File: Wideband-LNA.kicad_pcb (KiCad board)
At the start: 4 copper layers, 23.9 x 22.5 mm, 23 parts, among them J1 Conn_Coaxial, J2 Conn_Coaxial, J3 USB_C_Receptacle_USB2.0_16P, U1 TQP3M9037, U2 AP2127K-ADJ

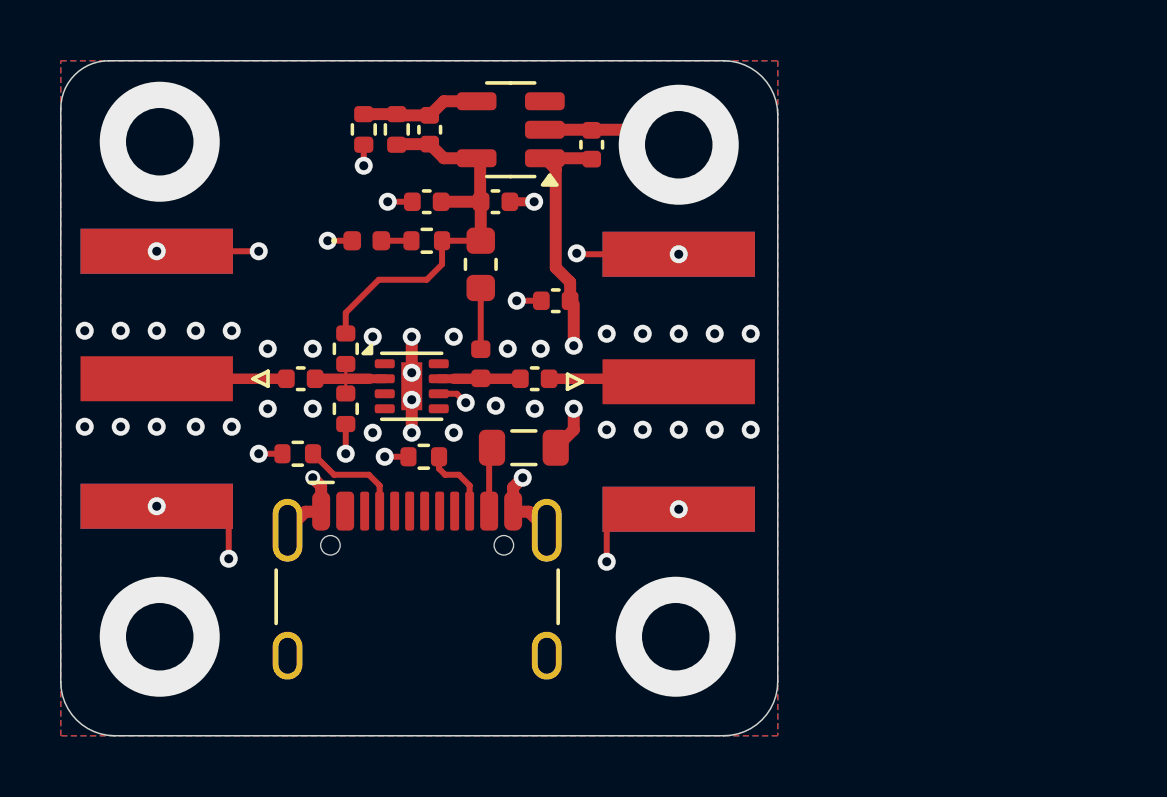
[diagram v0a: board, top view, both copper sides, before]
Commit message: rename datasheets, tweak layout
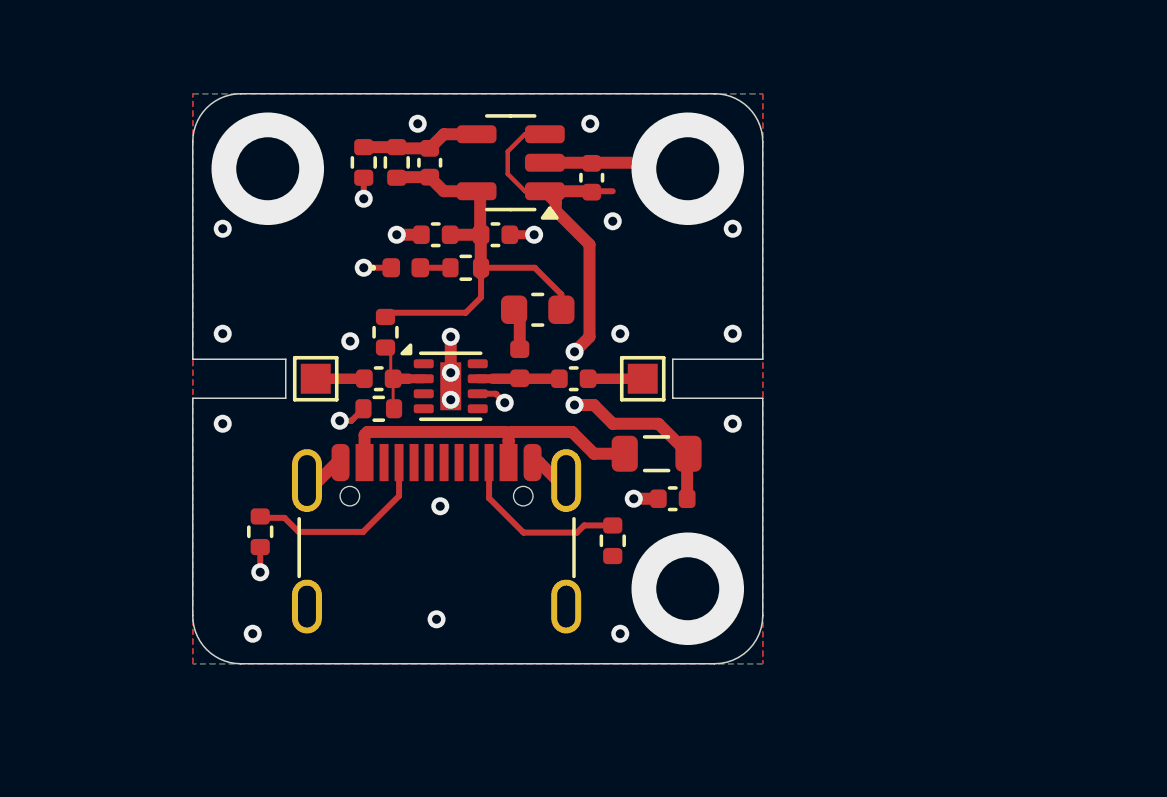
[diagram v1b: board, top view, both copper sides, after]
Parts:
- J1: value Conn_Coaxial -> RF-IN; footprint wa1hco:SMA_Amphenol_132289_EdgeMount -> TestPoint:TestPoint_Pad_1.0x1.0mm
- J2: value Conn_Coaxial -> RF-OUT; footprint wa1hco:SMA_Amphenol_132289_EdgeMount -> TestPoint:TestPoint_Pad_1.0x1.0mm
- J3: footprint Connector_USB:USB_C_Receptacle_HCTL_HC-TYPE-C-16P-01A -> wa1hco:USB_C_Receptacle_G-Switch_GT-USB-7010ASV
- moved C5 7.67 mm to (116.5, 104.0)
- moved R4 6.89 mm to (114.5, 105.4), turned to -90 degrees
- moved J1 5.30 mm to (104.6, 100.0), turned to 0 degrees
- moved FB1 4.43 mm to (116.0, 102.5)
- moved R3 2.88 mm to (102.8, 105.1), turned to -90 degrees
- moved C2 2.60 mm to (106.7, 100.0)
- moved L2 2.43 mm to (112.0, 97.7), turned to 180 degrees
- moved J3 1.76 mm to (108.6, 106.5)
- moved D1 1.58 mm to (107.6, 96.3)
- moved R2 1.58 mm to (109.6, 96.3)
- moved R7 1.43 mm to (106.9, 98.5)
- moved L1 1.30 mm to (111.4, 99.5)
- moved C1 1.30 mm to (113.2, 100.0)
- moved U1 1.30 mm to (109.1, 100.2)
- moved J2 1.20 mm to (115.5, 100.0)
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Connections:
- U2 pad 3: unconnected-(U2-EN-Pad3) -> /5V
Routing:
- net GND: track 33.1 -> 16.3 mm, vias 59 -> 29
- net Net-(FB1-Pad1): track 2.17 -> 10.9 mm
- net /5V: track 11.9 -> 20.0 mm
- net Net-(J3-CC2): track 2.52 -> 5.90 mm
- net Net-(J3-CC1): track 3.53 -> 6.47 mm
- net Net-(C2-Pad1): track 3.42 -> 1.62 mm
- net Net-(C1-Pad2): track 3.36 -> 1.86 mm
- net /4V75: track 13.4 -> 14.6 mm
- net Net-(L1-Pad1): track 2.04 -> 1.39 mm
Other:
- board size 23.9 x 22.5 mm -> 19 x 19 mm

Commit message: changed to 50 to 2000 MHz, qorvo 9036, 68 nH choke
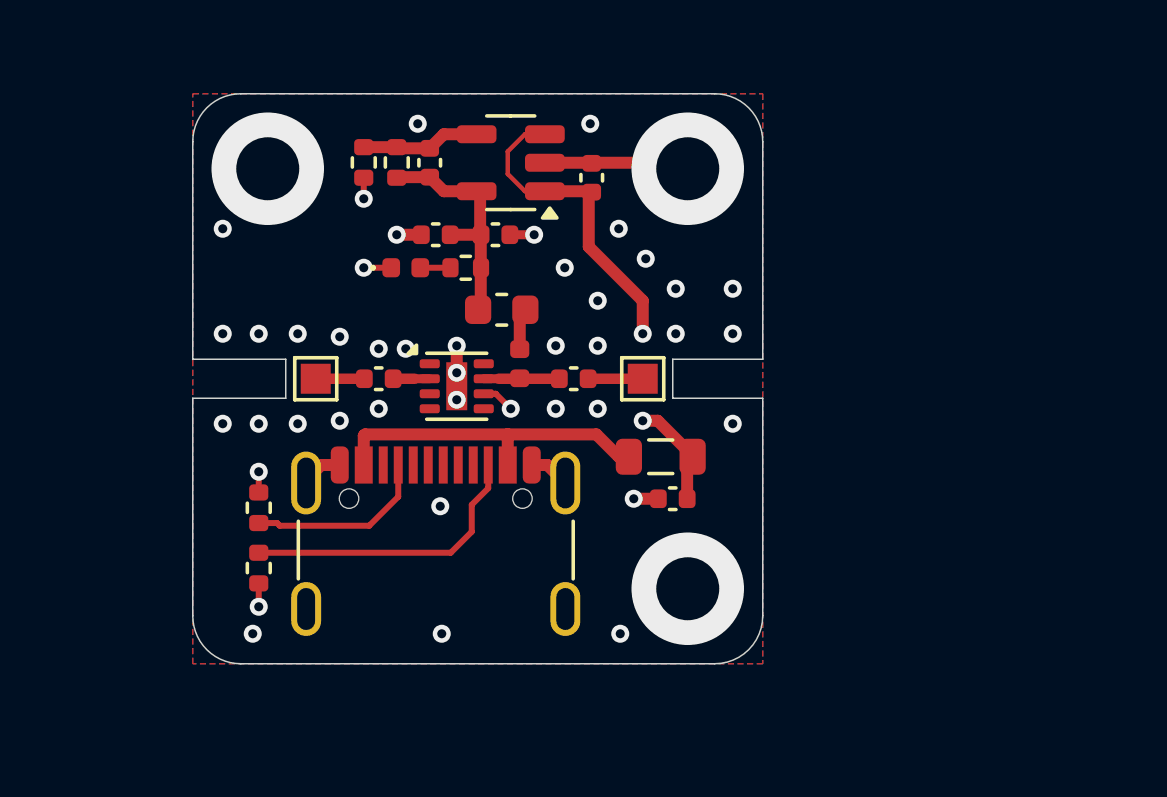
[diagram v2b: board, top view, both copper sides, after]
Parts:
- removed R1, R7: NP, Resistor_SMD:R_0402_1005Metric
- L2: value 18n -> 68n
- moved R4 11.8 mm to (102.7, 106.3)
- moved L2 1.20 mm to (110.8, 97.7), turned to 0 degrees
- moved R3 0.80 mm to (102.7, 104.3), turned to 90 degrees
- moved U1 0.20 mm to (109.3, 100.2)
- moved FB1 0.17 mm to (116.1, 102.6)
- moved J3 0.09 mm to (108.6, 106.6)
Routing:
- net /4V75: track 14.6 -> 7.83 mm
- net Net-(J3-CC2): track 5.90 -> 9.96 mm
- net /5V: track 20.0 -> 17.4 mm
- net Net-(U1-RFIN): track 3.18 -> 1.13 mm
- net GND: track 16.3 -> 15.4 mm, vias 29 -> 45

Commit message: M2 screw hole from via to mounting hole Increased radius of corners Reduced side to 18.8 mm to allow clearance in enclosure Increase size of notch for SMA pin Added into to back silkscreen
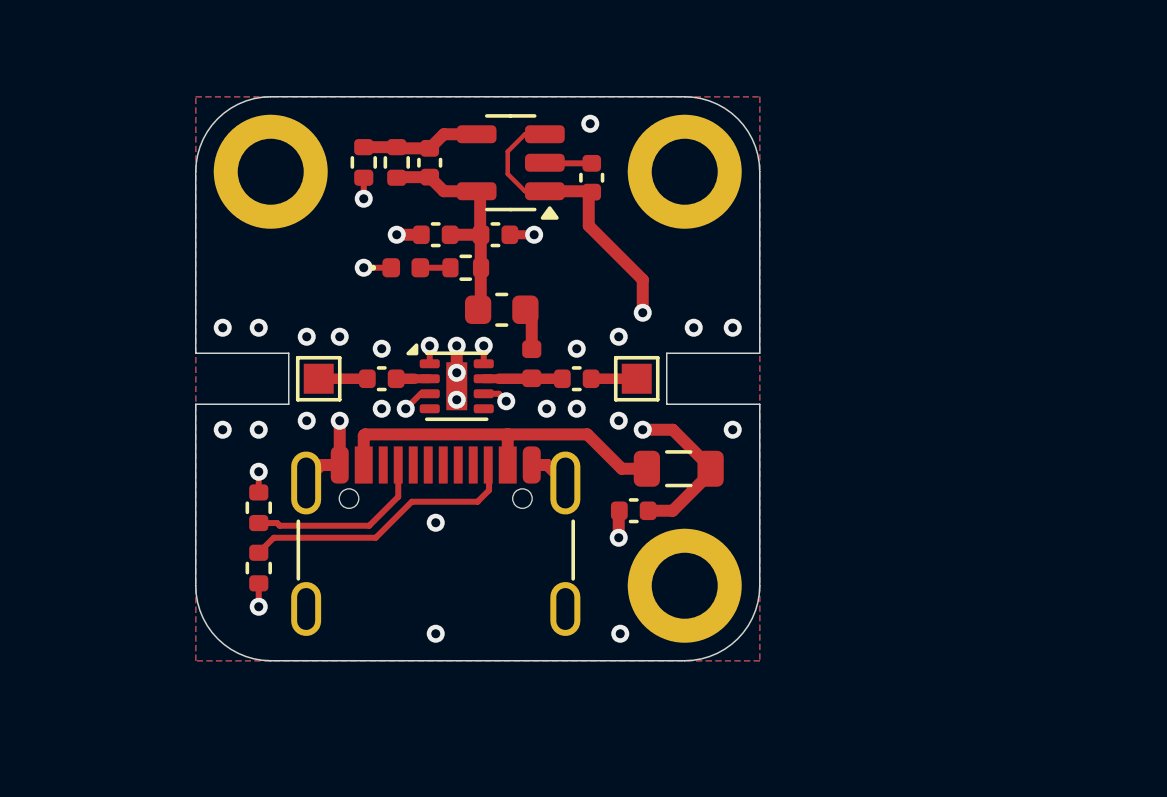
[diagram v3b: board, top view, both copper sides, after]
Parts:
- added H1: M2, MountingHole:MountingHole_2.2mm_M2_DIN965_Pad, F.Cu at (103.1, 93.1)
- added H2: M2, MountingHole:MountingHole_2.2mm_M2_DIN965_Pad, F.Cu at (116.9, 93.1)
- added H3: M2, MountingHole:MountingHole_2.2mm_M2_DIN965_Pad, F.Cu at (116.9, 106.9)
- U1: value TQP3M9037 -> TQP3M9036
- moved C5 1.36 mm to (115.2, 104.4)
- moved FB1 0.72 mm to (116.7, 103.0)
- moved L1 0.40 mm to (111.8, 99.5)
- moved J2 0.20 mm to (115.3, 100.0)
- moved J1 0.10 mm to (104.7, 100.0)
- moved C1 0.10 mm to (113.3, 100.0)
- moved C2 0.10 mm to (106.8, 100.0)
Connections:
- net /4V75 renamed /4V8
- U1 pad 1: (no net) -> GND
- U1 pad 3: (no net) -> GND
- U1 pad 4: (no net) -> GND
- U1 pad 5: (no net) -> GND
- U1 pad 8: (no net) -> GND
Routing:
- net /5V: track 17.4 -> 19.6 mm
- net Net-(FB1-Pad1): track 11.2 -> 11.9 mm
- net GND: vias 45 -> 36
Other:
- board size 19 x 19 mm -> 18.8 x 18.8 mm
- board text added: "LNA 50-2000 MHz (c) wa1hco Creative Commons License V4 Attribute and Share Alike"

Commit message: added SO323 diodes to input for protection.  Added experiment for power over coax. Added id and copyright to back silkscreen. changed screw vias to mounting holes reduced size to 18.8 x 18.8 mm for tolerance.
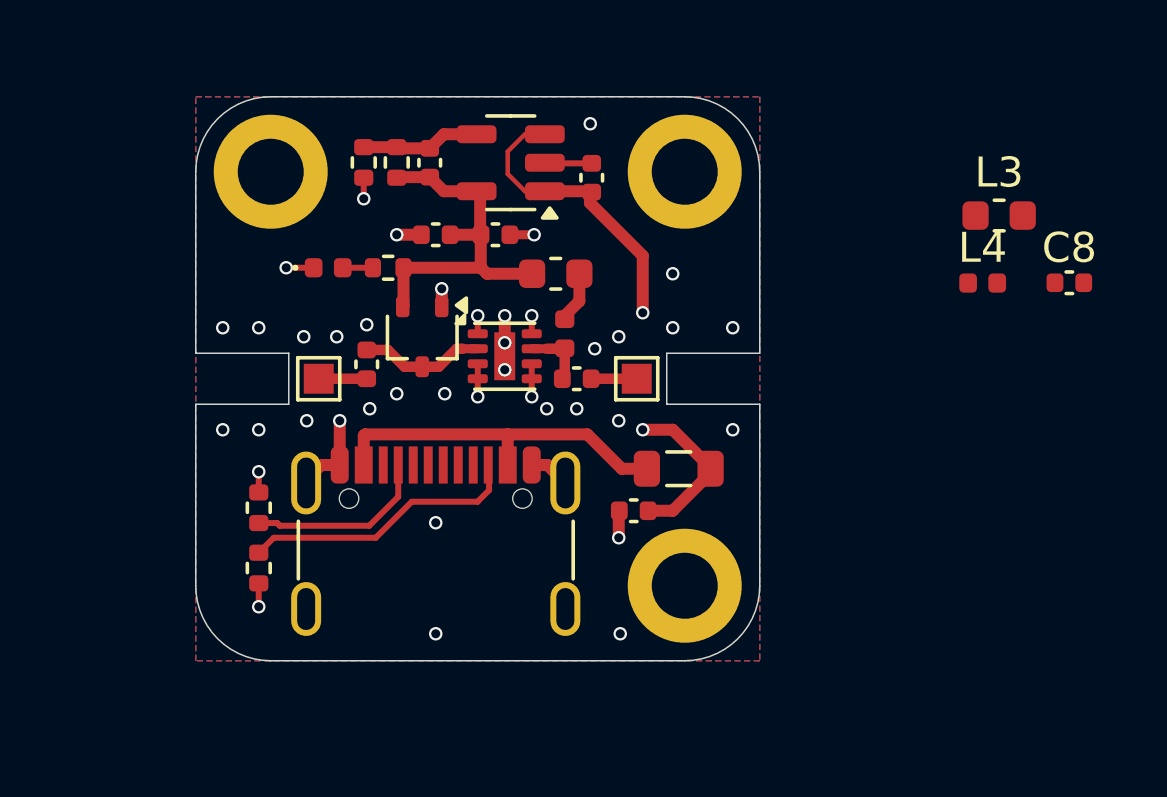
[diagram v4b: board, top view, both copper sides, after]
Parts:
- added C8: 100p, Capacitor_SMD:C_0402_1005Metric, F.Cu at (129.7, 96.8)
- added D2: BAT54SW, Package_TO_SOT_SMD:SOT-323_SC-70, F.Cu at (108.2, 98.6)
- added L3: 68n, Inductor_SMD:L_0603_1608Metric, F.Cu at (127.4, 94.6)
- added L4: 4n7, Inductor_SMD:L_0402_1005Metric, F.Cu at (126.8, 96.8)
- moved D1 2.58 mm to (105.0, 96.3)
- moved R2 2.58 mm to (107.0, 96.3)
- moved L2 2.16 mm to (112.6, 96.5)
- moved U1 1.89 mm to (110.9, 99.2)
- moved L1 1.49 mm to (112.9, 98.5)
- moved C2 0.69 mm to (106.3, 99.5), turned to 90 degrees
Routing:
- net /4V8: track 7.83 -> 12.1 mm
- net Net-(D2-COM): track 1.23 -> 4.18 mm
- net GND: track 15.4 -> 16.3 mm, vias 36 -> 40

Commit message: Added power over output coax, forwarding to USB-C Changed input protection from OVP diodes to Inductor to ground.
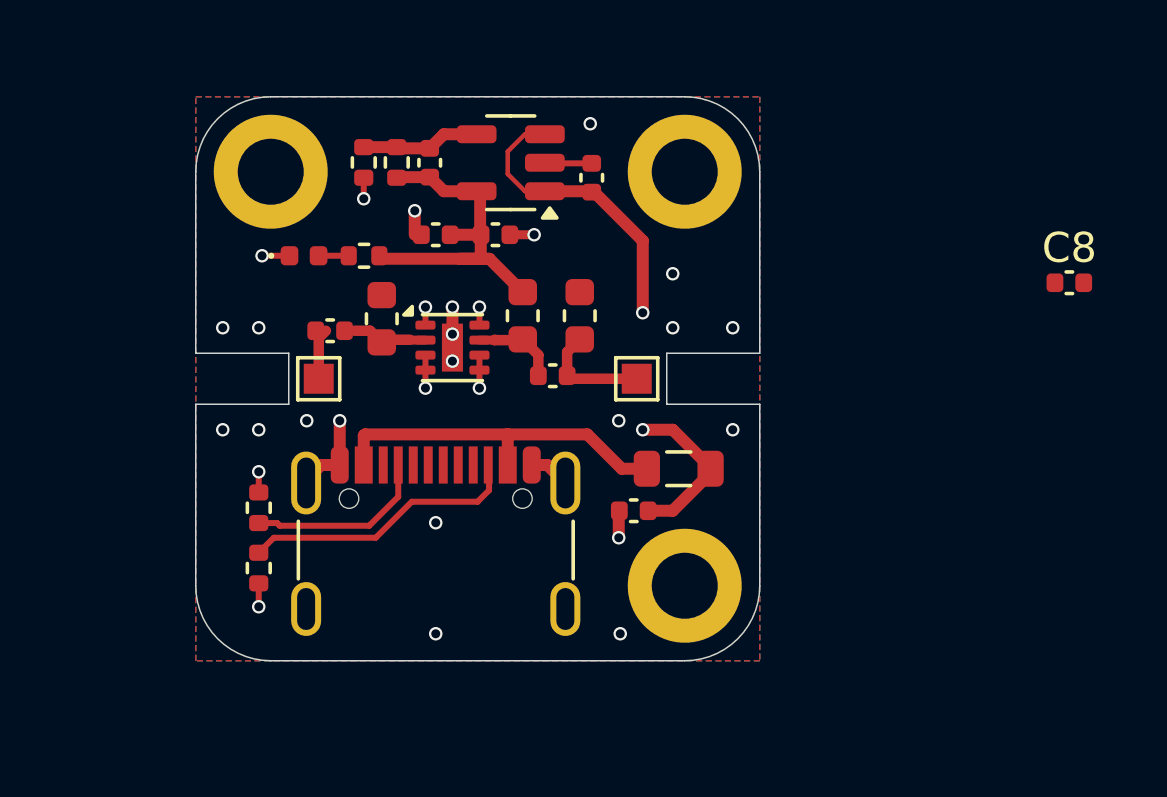
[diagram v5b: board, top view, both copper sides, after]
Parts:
- removed D2: BAT54SW, Package_TO_SOT_SMD:SOT-323_SC-70
- removed L4: 4n7, Inductor_SMD:L_0402_1005Metric
- L1: value 4n7 -> 68n; footprint Inductor_SMD:L_0402_1005Metric -> Inductor_SMD:L_0603_1608Metric
- moved L3 14.4 mm to (113.4, 97.9), turned to -90 degrees
- moved L1 6.12 mm to (106.8, 98.0), turned to 90 degrees
- moved L2 1.78 mm to (111.5, 97.9), turned to -90 degrees
- moved U1 1.77 mm to (109.2, 99.0)
- moved C2 1.66 mm to (105.1, 98.4), turned to 0 degrees
- moved D1 0.90 mm to (104.2, 95.9)
- moved R2 0.90 mm to (106.2, 95.9)
- moved C1 0.81 mm to (112.5, 99.9)
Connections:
- C2 pad 2: Net-(D2-COM) -> Net-(U1-RFIN)
- L1 pad 1: Net-(L1-Pad1) -> Net-(U1-RFIN)
- L1 pad 2: Net-(U1-RFOUT) -> GND
- L2 pad 2: Net-(L1-Pad1) -> Net-(U1-RFOUT)
- L3 pad 2: Net-(L3-Pad2) -> Net-(C1-Pad2)
- U1 pad 2: Net-(D2-COM) -> Net-(U1-RFIN)
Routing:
- net Net-(D2-COM): track 4.18 -> 0.00 mm
- net Net-(U1-RFIN): track 0.00 -> 2.67 mm
- net Net-(C1-Pad2): track 1.52 -> 3.75 mm
- net Net-(L1-Pad1): track 1.72 -> 0.00 mm
- net Net-(U1-RFOUT): track 2.15 -> 2.90 mm
- net GND: track 16.3 -> 15.9 mm, vias 40 -> 29
